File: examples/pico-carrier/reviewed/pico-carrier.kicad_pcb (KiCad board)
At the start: 2 copper layers, 82 x 68 mm, 9 parts, among them J1 5V IN, J3 GP0-GP15, J4 GP16-GP28, PWR, U1 Pico

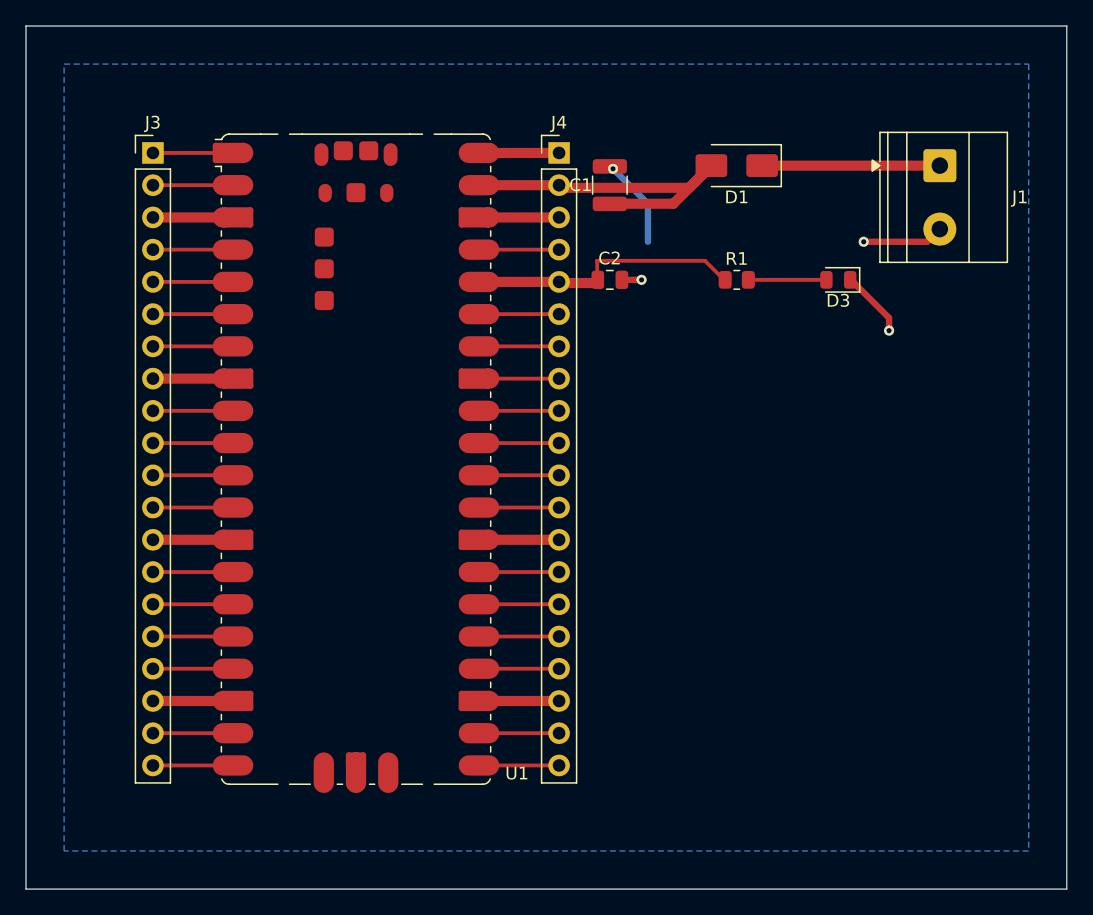
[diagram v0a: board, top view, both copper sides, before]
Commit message: Regenerate the five with stitched pours, silk that speaks, and wires that never double back
All ten variants rebuilt by the fixed generator: reviewed boards carry
ground on both faces with the stitching ring (buck 35 vias, fpga 116),
thru_hole_only front pours, the board id and connector pin names in
silk, and the buck's explicit ground return; the sheets hook power up
through upright symbols and source-anchored flags with no overlapping
wires and no junction-less tees left. Every reviewed variant passes its
own gate with zero errors; every as-generated variant still fails, now
also for the rules this round added.

Co-Authored-By: Claude Fable 5 <noreply@anthropic.com>
Claude-Session: https://claude.ai/code/session_01DUj7Ltu92tWg159mCSacwY
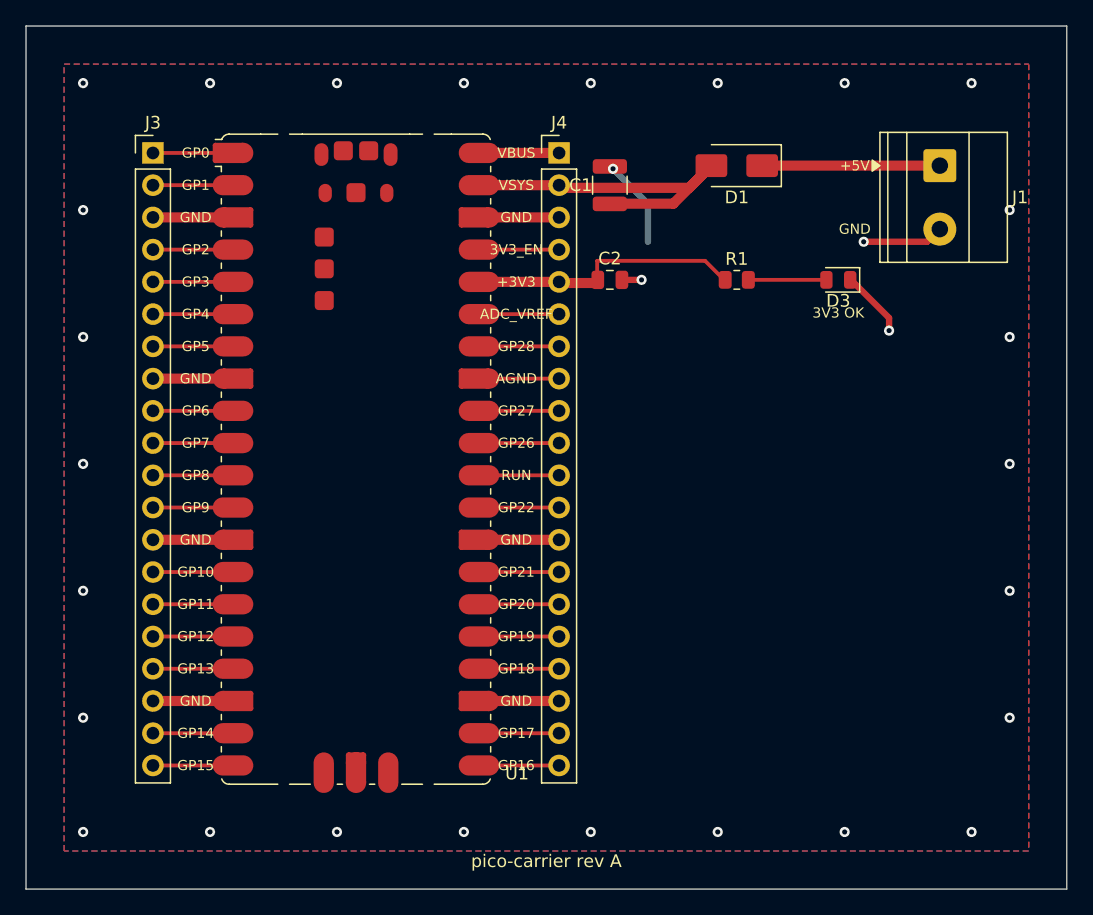
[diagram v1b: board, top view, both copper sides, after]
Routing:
- net GND: vias 4 -> 30
- added copper zone on F.Cu, net GND
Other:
- board text added: "+3V3"
- board text added: "+5V"
- board text added: "3V3 OK"
- board text added: "3V3_EN"
- board text added: "ADC_VREF"
- board text added: "AGND"
- board text added: "GND"
- board text added: "GP0"
- board text added: "GP1"
- board text added: "GP10"
- board text added: "GP11"
- board text added: "GP12"
- board text added: "GP13"
- board text added: "GP14"
- board text added: "GP15"
- board text added: "GP16"
- board text added: "GP17"
- board text added: "GP18"
- board text added: "GP19"
- board text added: "GP2"
- board text added: "GP20"
- board text added: "GP21"
- board text added: "GP22"
- board text added: "GP26"
- board text added: "GP27"
- board text added: "GP28"
- board text added: "GP3"
- board text added: "GP4"
- board text added: "GP5"
- board text added: "GP6"
- board text added: "GP7"
- board text added: "GP8"
- board text added: "GP9"
- board text added: "RUN"
- board text added: "VBUS"
- board text added: "VSYS"
- board text added: "pico-carrier rev A"
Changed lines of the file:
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@@
 	(via (at 168.0 84.0) (size 0.8) (drill 0.4) (layers "F.Cu" "B.Cu") (net 1))
 	(via (at 166.0 77.0) (size 0.8) (drill 0.4) (layers "F.Cu" "B.Cu") (net 1))
+	(via (at 104.5 64.5) (size 0.8) (drill 0.4) (layers "F.Cu" "B.Cu") (net 1))
+	(via (at 104.5 123.5) (size 0.8) (drill 0.4) (layers "F.Cu" "B.Cu") (net 1))
+	(via (at 114.5 64.5) (size 0.8) (drill 0.4) (layers "F.Cu" "B.Cu") (net 1))
+	(via (at 114.5 123.5) (size 0.8) (drill 0.4) (layers "F.Cu" "B.Cu") (net 1))
+	(via (at 124.5 64.5) (size 0.8) (drill 0.4) (layers "F.Cu" "B.Cu") (net 1))
+	(via (at 124.5 123.5) (size 0.8) (drill 0.4) (layers "F.Cu" "B.Cu") (net 1))
+	(via (at 134.5 64.5) (size 0.8) (drill 0.4) (layers "F.Cu" "B.Cu") (net 1))
+	(via (at 134.5 123.5) (size 0.8) (drill 0.4) (layers "F.Cu" "B.Cu") (net 1))
+	(via (at 144.5 64.5) (size 0.8) (drill 0.4) (layers "F.Cu" "B.Cu") (net 1))
+	(via (at 144.5 123.5) (size 0.8) (drill 0.4) (layers "F.Cu" "B.Cu") (net 1))
+	(via (at 154.5 64.5) (size 0.8) (drill 0.4) (layers "F.Cu" "B.Cu") (net 1))
+	(via (at 154.5 123.5) (size 0.8) (drill 0.4) (layers "F.Cu" "B.Cu") (net 1))
+	(via (at 164.5 64.5) (size 0.8) (drill 0.4) (layers "F.Cu" "B.Cu") (net 1))
+	(via (at 164.5 123.5) (size 0.8) (drill 0.4) (layers "F.Cu" "B.Cu") (net 1))
+	(via (at 174.5 64.5) (size 0.8) (drill 0.4) (layers "F.Cu" "B.Cu") (net 1))
+	(via (at 174.5 123.5) (size 0.8) (drill 0.4) (layers "F.Cu" "B.Cu") (net 1))
+	(via (at 104.5 74.5) (size 0.8) (drill 0.4) (layers "F.Cu" "B.Cu") (net 1))
+	(via (at 177.5 74.5) (size 0.8) (drill 0.4) (layers "F.Cu" "B.Cu") (net 1))
+	(via (at 104.5 84.5) (size 0.8) (drill 0.4) (layers "F.Cu" "B.Cu") (net 1))
+	(via (at 177.5 84.5) (size 0.8) (drill 0.4) (layers "F.Cu" "B.Cu") (net 1))
+	(via (at 104.5 94.5) (size 0.8) (drill 0.4) (layers "F.Cu" "B.Cu") (net 1))
+	(via (at 177.5 94.5) (size 0.8) (drill 0.4) (layers "F.Cu" "B.Cu") (net 1))
+	(via (at 104.5 104.5) (size 0.8) (drill 0.4) (layers "F.Cu" "B.Cu") (net 1))
+	(via (at 177.5 104.5) (size 0.8) (drill 0.4) (layers "F.Cu" "B.Cu") (net 1))
+	(via (at 104.5 114.5) (size 0.8) (drill 0.4) (layers "F.Cu" "B.Cu") (net 1))
+	(via (at 177.5 114.5) (size 0.8) (drill 0.4) (layers "F.Cu" "B.Cu") (net 1))
 	(zone
 		(net 1)
@@
 		(polygon (pts (xy 103.0 63.0) (xy 179.0 63.0) (xy 179.0 125.0) (xy 103.0 125.0)))
 	)
+	(zone
+		(net 1)
+		(net_name "GND")
+		(layer "F.Cu")
+		(hatch edge 0.5)
+		(connect_pads thru_hole_only
+			(clearance 0.4)
+		)
+		(min_thickness 0.175)
+		(filled_areas_thickness no)
+		(fill yes
+			(thermal_gap 0.5)
+			(thermal_bridge_width 0.5)
+		)
+		(polygon (pts (xy 103.0 63.0) (xy 179.0 63.0) (xy 179.0 125.0) (xy 103.0 125.0)))
+	)
+	(gr_text "pico-carrier rev A" (at 141.0 125.8 0) (layer "F.SilkS") (effects (font (size 1.0 1.0) (thickness 0.15))))
+	(gr_text "GP0" (at 113.37 70.0 0) (layer "F.SilkS") (effects (font (size 0.8 0.8) (thickness 0.12))))
+	(gr_text "GP1" (at 113.37 72.54 0) (layer "F.SilkS") (effects (font (size 0.8 0.8) (thickness 0.12))))
+	(gr_text "GND" (at 113.37 75.08 0) (layer "F.SilkS") (effects (font (size 0.8 0.8) (thickness 0.12))))
+	(gr_text "GP2" (at 113.37 77.62 0) (layer "F.SilkS") (effects (font (size 0.8 0.8) (thickness 0.12))))
+	(gr_text "GP3" (at 113.37 80.16 0) (layer "F.SilkS") (effects (font (size 0.8 0.8) (thickness 0.12))))
+	(gr_text "GP4" (at 113.37 82.7 0) (layer "F.SilkS") (effects (font (size 0.8 0.8) (thickness 0.12))))
+	(gr_text "GP5" (at 113.37 85.24 0) (layer "F.SilkS") (effects (font (size 0.8 0.8) (thickness 0.12))))
+	(gr_text "GND" (at 113.37 87.78 0) (layer "F.SilkS") (effects (font (size 0.8 0.8) (thickness 0.12))))
+	(gr_text "GP6" (at 113.37 90.32 0) (layer "F.SilkS") (effects (font (size 0.8 0.8) (thickness 0.12))))
+	(gr_text "GP7" (at 113.37 92.86 0) (layer "F.SilkS") (effects (font (size 0.8 0.8) (thickness 0.12))))
+	(gr_text "GP8" (at 113.37 95.4 0) (layer "F.SilkS") (effects (font (size 0.8 0.8) (thickness 0.12))))
+	(gr_text "GP9" (at 113.37 97.94 0) (layer "F.SilkS") (effects (font (size 0.8 0.8) (thickness 0.12))))
+	(gr_text "GND" (at 113.37 100.48 0) (layer "F.SilkS") (effects (font (size 0.8 0.8) (thickness 0.12))))
+	(gr_text "GP10" (at 113.37 103.02 0) (layer "F.SilkS") (effects (font (size 0.8 0.8) (thickness 0.12))))
+	(gr_text "GP11" (at 113.37 105.56 0) (layer "F.SilkS") (effects (font (size 0.8 0.8) (thickness 0.12))))
+	(gr_text "GP12" (at 113.37 108.1 0) (layer "F.SilkS") (effects (font (size 0.8 0.8) (thickness 0.12))))
+	(gr_text "GP13" (at 113.37 110.64 0) (layer "F.SilkS") (effects (font (size 0.8 0.8) (thickness 0.12))))
+	(gr_text "GND" (at 113.37 113.18 0) (layer "F.SilkS") (effects (font (size 0.8 0.8) (thickness 0.12))))
+	(gr_text "GP14" (at 113.37 115.72 0) (layer "F.SilkS") (effects (font (size 0.8 0.8) (thickness 0.12))))
+	(gr_text "GP15" (at 113.37 118.26 0) (layer "F.SilkS") (effects (font (size 0.8 0.8) (thickness 0.12))))
+	(gr_text "VBUS" (at 138.63 70.0 0) (layer "F.SilkS") (effects (font (size 0.8 0.8) (thickness 0.12))))
+	(gr_text "VSYS" (at 138.63 72.54 0) (layer "F.SilkS") (effects (font (size 0.8 0.8) (thickness 0.12))))
+	(gr_text "GND" (at 138.63 75.08 0) (layer "F.SilkS") (effects (font (size 0.8 0.8) (thickness 0.12))))
+	(gr_text "3V3_EN" (at 138.63 77.62 0) (layer "F.SilkS") (effects (font (size 0.8 0.8) (thickness 0.12))))
+	(gr_text "+3V3" (at 138.63 80.16 0) (layer "F.SilkS") (effects (font (size 0.8 0.8) (thickness 0.12))))
+	(gr_text "ADC_VREF" (at 138.63 82.7 0) (layer "F.SilkS") (effects (font (size 0.8 0.8) (thickness 0.12))))
+	(gr_text "GP28" (at 138.63 85.24 0) (layer "F.SilkS") (effects (font (size 0.8 0.8) (thickness 0.12))))
+	(gr_text "AGND" (at 138.63 87.78 0) (layer "F.SilkS") (effects (font (size 0.8 0.8) (thickness 0.12))))
+	(gr_text "GP27" (at 138.63 90.32 0) (layer "F.SilkS") (effects (font (size 0.8 0.8) (thickness 0.12))))
+	(gr_text "GP26" (at 138.63 92.86 0) (layer "F.SilkS") (effects (font (size 0.8 0.8) (thickness 0.12))))
+	(gr_text "RUN" (at 138.63 95.4 0) (layer "F.SilkS") (effects (font (size 0.8 0.8) (thickness 0.12))))
+	(gr_text "GP22" (at 138.63 97.94 0) (layer "F.SilkS") (effects (font (size 0.8 0.8) (thickness 0.12))))
+	(gr_text "GND" (at 138.63 100.48 0) (layer "F.SilkS") (effects (font (size 0.8 0.8) (thickness 0.12))))
+	(gr_text "GP21" (at 138.63 103.02 0) (layer "F.SilkS") (effects (font (size 0.8 0.8) (thickness 0.12))))
+	(gr_text "GP20" (at 138.63 105.56 0) (layer "F.SilkS") (effects (font (size 0.8 0.8) (thickness 0.12))))
+	(gr_text "GP19" (at 138.63 108.1 0) (layer "F.SilkS") (effects (font (size 0.8 0.8) (thickness 0.12))))
+	(gr_text "GP18" (at 138.63 110.64 0) (layer "F.SilkS") (effects (font (size 0.8 0.8) (thickness 0.12))))
+	(gr_text "GND" (at 138.63 113.18 0) (layer "F.SilkS") (effects (font (size 0.8 0.8) (thickness 0.12))))
+	(gr_text "GP17" (at 138.63 115.72 0) (layer "F.SilkS") (effects (font (size 0.8 0.8) (thickness 0.12))))
+	(gr_text "GP16" (at 138.63 118.26 0) (layer "F.SilkS") (effects (font (size 0.8 0.8) (thickness 0.12))))
+	(gr_text "+5V" (at 165.3 71.0 0) (layer "F.SilkS") (effects (font (size 0.8 0.8) (thickness 0.12))))
+	(gr_text "GND" (at 165.3 76.0 0) (layer "F.SilkS") (effects (font (size 0.8 0.8) (thickness 0.12))))
+	(gr_text "3V3 OK" (at 164.0 82.6 0) (layer "F.SilkS") (effects (font (size 0.8 0.8) (thickness 0.12))))
 )

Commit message: Regenerate the five as round three drew them
All five reviewed projects pass their gates again: the buck all wire
with its feedback drawn home, the motor's logic named at the header,
the carrier reading as the pinout table it is - with its feed diode
finally pointing the right way - the filter compact with test points,
and the FPGA's capacitors sitting beside the units they feed. Thirty
renders redrawn, verdict tables at today's numbers.

Co-Authored-By: Claude Fable 5 <noreply@anthropic.com>
Claude-Session: https://claude.ai/code/session_01DUj7Ltu92tWg159mCSacwY
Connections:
- D1 pad 1: +5V -> /VSYS
- D1 pad 2: /VSYS -> +5V
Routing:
- net /VSYS: track 28.4 -> 36.6 mm
- net +5V: track 14.0 -> 19.7 mm
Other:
- board text added: "kicad_skills examples"
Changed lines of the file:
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@@
       (layers "F.Cu" "F.Mask" "F.Paste")
       (roundrect_rratio 0.1388888889)
-      (net 3 "+5V")
+      (net 36 "/VSYS")
     )
     (pad "2" smd roundrect
@@
       (layers "F.Cu" "F.Mask" "F.Paste")
       (roundrect_rratio 0.1388888889)
-      (net 36 "/VSYS")
+      (net 3 "+5V")
     )
     (embedded_fonts no)
@@
 	(segment (start 135.69 115.72) (end 142.0 115.72) (width 0.3) (layer "F.Cu") (net 16))
 	(segment (start 135.69 118.26) (end 142.0 118.26) (width 0.3) (layer "F.Cu") (net 15))
-	(segment (start 172.0 71.0) (end 158.0 71.0) (width 0.8) (layer "F.Cu") (net 3))
-	(segment (start 154.0 71.0) (end 152.25 72.75) (width 0.8) (layer "F.Cu") (net 36))
-	(segment (start 152.25 72.75) (end 142.25 72.75) (width 0.8) (layer "F.Cu") (net 36))
+	(segment (start 172.0 71.0) (end 170.0 69.0) (width 0.8) (layer "F.Cu") (net 3))
+	(segment (start 170.0 69.0) (end 156.0 69.0) (width 0.8) (layer "F.Cu") (net 3))
+	(segment (start 156.0 69.0) (end 154.0 71.0) (width 0.8) (layer "F.Cu") (net 3))
+	(segment (start 158.0 71.0) (end 156.0 73.0) (width 0.8) (layer "F.Cu") (net 36))
+	(segment (start 156.0 73.0) (end 142.5 73.0) (width 0.8) (layer "F.Cu") (net 36))
+	(segment (start 142.5 73.0) (end 142.25 72.75) (width 0.8) (layer "F.Cu") (net 36))
 	(segment (start 142.25 72.75) (end 142.0 72.54) (width 0.8) (layer "F.Cu") (net 36))
 	(segment (start 146.0 74.015) (end 146.25 74.0) (width 0.8) (layer "F.Cu") (net 36))
-	(segment (start 146.25 74.0) (end 151.0 74.0) (width 0.8) (layer "F.Cu") (net 36))
-	(segment (start 151.0 74.0) (end 154.0 71.0) (width 0.8) (layer "F.Cu") (net 36))
+	(segment (start 146.25 74.0) (end 155.0 74.0) (width 0.8) (layer "F.Cu") (net 36))
+	(segment (start 155.0 74.0) (end 158.0 71.0) (width 0.8) (layer "F.Cu") (net 36))
 	(segment (start 145.05 80.0) (end 144.75 80.25) (width 0.8) (layer "F.Cu") (net 2))
 	(segment (start 144.75 80.25) (end 142.25 80.25) (width 0.8) (layer "F.Cu") (net 2))
 	(segment (start 142.25 80.25) (end 142.0 80.16) (width 0.8) (layer "F.Cu") (net 2))
 	(segment (start 145.05 80.0) (end 145.0 79.75) (width 0.3) (layer "F.Cu") (net 2))
-	(segment (start 145.0 79.75) (end 145.0 78.5) (width 0.3) (layer "F.Cu") (net 2))
-	(segment (start 145.0 78.5) (end 153.5 78.5) (width 0.3) (layer "F.Cu") (net 2))
+	(segment (start 145.0 79.75) (end 145.0 79.125) (width 0.3) (layer "F.Cu") (net 2))
+	(segment (start 145.0 79.125) (end 145.625 78.5) (width 0.3) (layer "F.Cu") (net 2))
+	(segment (start 145.625 78.5) (end 153.5 78.5) (width 0.3) (layer "F.Cu") (net 2))
 	(segment (start 153.5 78.5) (end 154.75 79.75) (width 0.3) (layer "F.Cu") (net 2))
 	(segment (start 154.75 79.75) (end 155.0875 80.0) (width 0.3) (layer "F.Cu") (net 2))
 	(segment (start 156.9125 80.0) (end 163.0625 80.0) (width 0.3) (layer "F.Cu") (net 33))
 	(segment (start 146.0 71.065) (end 146.25 71.25) (width 0.5) (layer "F.Cu") (net 1))
-	(segment (start 146.25 71.25) (end 149.0 74.0) (width 0.5) (layer "B.Cu") (net 1))
+	(segment (start 146.25 71.25) (end 146.5 71.5) (width 0.5) (layer "F.Cu") (net 1))
+	(segment (start 146.5 71.5) (end 149.0 74.0) (width 0.5) (layer "B.Cu") (net 1))
 	(segment (start 149.0 74.0) (end 149.0 77.0) (width 0.5) (layer "B.Cu") (net 1))
 	(segment (start 146.95 80.0) (end 148.5 80.0) (width 0.5) (layer "F.Cu") (net 1))
@@
 	(segment (start 172.0 76.0) (end 171.0 77.0) (width 0.5) (layer "F.Cu") (net 1))
 	(segment (start 171.0 77.0) (end 166.0 77.0) (width 0.5) (layer "F.Cu") (net 1))
-	(via (at 146.25 71.25) (size 0.8) (drill 0.4) (layers "F.Cu" "B.Cu") (net 1))
+	(via (at 146.5 71.5) (size 0.8) (drill 0.4) (layers "F.Cu" "B.Cu") (net 1))
 	(via (at 148.5 80.0) (size 0.8) (drill 0.4) (layers "F.Cu" "B.Cu") (net 1))
 	(via (at 168.0 84.0) (size 0.8) (drill 0.4) (layers "F.Cu" "B.Cu") (net 1))
@@
 		(polygon (pts (xy 103.0 63.0) (xy 179.0 63.0) (xy 179.0 125.0) (xy 103.0 125.0)))
 	)
-	(gr_text "pico-carrier rev A" (at 141.0 125.8 0) (layer "F.SilkS") (effects (font (size 1.0 1.0) (thickness 0.15))))
+	(gr_text "pico-carrier rev A" (at 141.0 123.6 0) (layer "F.SilkS") (effects (font (size 1.2 1.2) (thickness 0.18))))
+	(gr_text "kicad_skills examples" (at 141.0 126.0 0) (layer "F.SilkS") (effects (font (size 1.0 1.0) (thickness 0.15))))
 	(gr_text "GP0" (at 113.37 70.0 0) (layer "F.SilkS") (effects (font (size 0.8 0.8) (thickness 0.12))))
 	(gr_text "GP1" (at 113.37 72.54 0) (layer "F.SilkS") (effects (font (size 0.8 0.8) (thickness 0.12))))

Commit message: Regenerate the four boards round four has settled
The buck, the motor driver, the carrier and the filter as the current
generator draws them: interior ground stitching on all four, the motor
driver's bundle tight and its board twelve millimetres shorter, the
filter compact and hand-placed, the carrier's indicator in a column of
its own. All four pass their gates. The FPGA is still regenerating.

Co-Authored-By: Claude Fable 5 <noreply@anthropic.com>
Claude-Session: https://claude.ai/code/session_01DUj7Ltu92tWg159mCSacwY
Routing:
- net GND: vias 30 -> 190
